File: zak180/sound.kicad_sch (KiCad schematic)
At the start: 1 part, among them U3 PSG_AY-3-8912

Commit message: HW: Further work on schematic
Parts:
- added C23, C24, C25, C26: 100n, Capacitor_THT:C_Disc_D5.0mm_W2.5mm_P2.50mm, symbol Device:C
- added C27: 47n, Capacitor_THT:C_Disc_D5.0mm_W2.5mm_P2.50mm, symbol Device:C
- added C28, C30, C31: 150u, symbol Device:C_Polarized
- added C29: 22u, symbol Device:C_Polarized
- added J4: Conn_01x02_Pin, Connector_PinHeader_1.00mm:PinHeader_1x02_P1.00mm_Vertical, symbol Connector:Conn_01x02_Pin
- added R26, R27, R28: 2K2, Resistor_THT:R_Axial_DIN0207_L6.3mm_D2.5mm_P7.62mm_Horizontal, symbol Device:R
- added R29: 10R, Resistor_THT:R_Axial_DIN0207_L6.3mm_D2.5mm_P7.62mm_Horizontal, symbol Device:R
- added RV1: 1K, symbol Device:R_Potentiometer
- added U11: 74HC02, Package_DIP:DIP-14_W7.62mm, symbol 74xx:74HC02
- added U16: 74HC08, Package_DIP:DIP-14_W7.62mm, symbol 74xx:74LS08
- added U17: LM386, symbol Amplifier_Audio:LM386
- U3: footprint (none) -> Package_DIP:DIP-28_W15.24mm
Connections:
- net GND: now also C23.2, C24.2, C25.2, C26.2, C30.1, C31.1, J4.1 (Pin_1), R29.1, RV1.3, U11.7 (GND), U16.7 (GND), U17.2 (-), U17.4 (GND)
- net VCC: now also U3.17 (A8), U3.19 (BC2), C23.1, C24.1, C25.1, C26.1, C30.2, C31.2, U11.14 (VCC), U16.14 (VCC), U17.6 (V+)
- net at U3.1 (ch_C): now also R28.1
- net SCRL4: now reaches U3.10 (IOA4)
- net SCRL3: now reaches U3.11 (IOA3)
- net SCRL2: now reaches U3.12 (IOA2)
- net SCRL1: now reaches U3.13 (IOA1)
- net SCRL0: now reaches U3.14 (IOA0)
- net CLK: now reaches U3.15 (CLOCK)
- net ~{RST}: now reaches U3.16 (~{RESET})
- net at U3.18 (BDIR): now also U11.1
- net at U3.20 (BC1): now also U11.13
- net at U3.4 (ch_B): now also R27.1
- net at U3.5 (ch_A): now also R26.1
- net ROMSEL1: now reaches U3.7 (IOA7)
- net ROMSEL0: now reaches U3.8 (IOA6)
- net SCRL5: now reaches U3.9 (IOA5)
- new net: R26.2, R27.2, R28.2, RV1.1
- new net: C29.1, RV1.2
- new net: U11.12, U16.3
- new net: C28.2, J4.2 (Pin_2)
- new net: C27.2, R29.2
- new net: C29.2, U17.3 (+)
- new net: C27.1, C28.1, U17.5
- new net: U11.10, U11.11
- new net: U11.4, U11.8, U11.9
- new net A0: U11.6
- new net ~{CS}: U11.3, U11.5
- new net ~{RD}: U16.2
- new net ~{WR}: U11.2, U16.1
- no-connect marks 0 -> 4

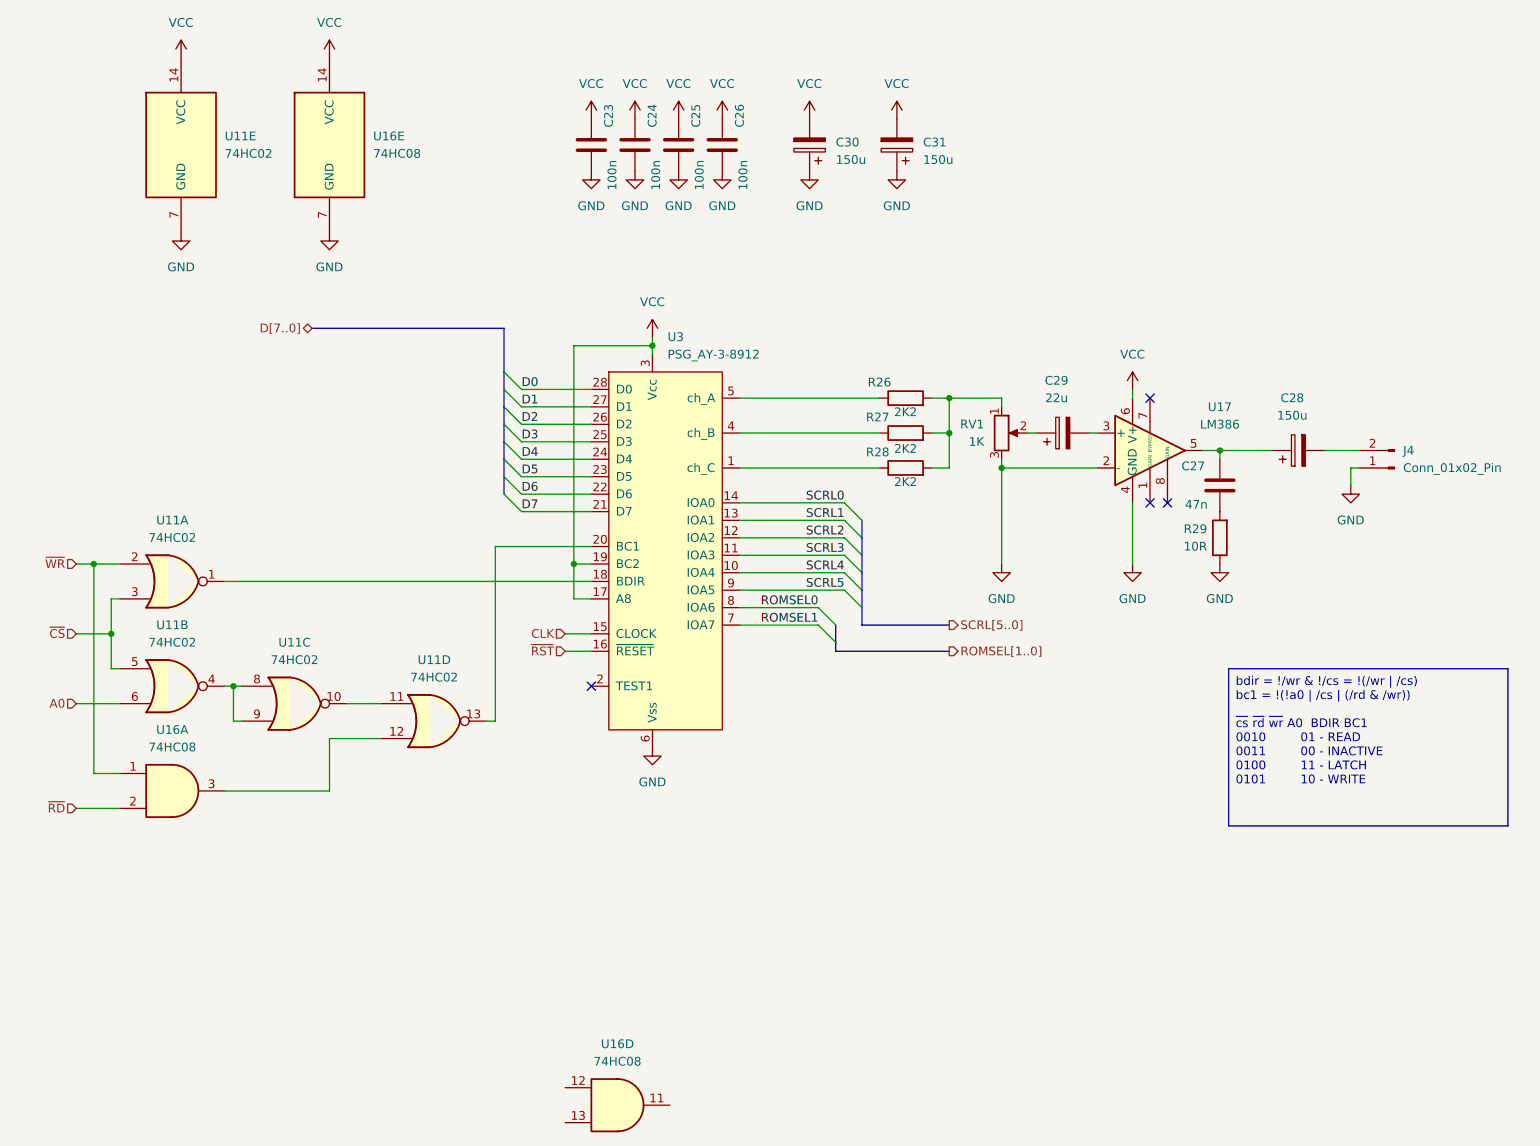
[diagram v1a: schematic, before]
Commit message: HW: Add memory, serial and power
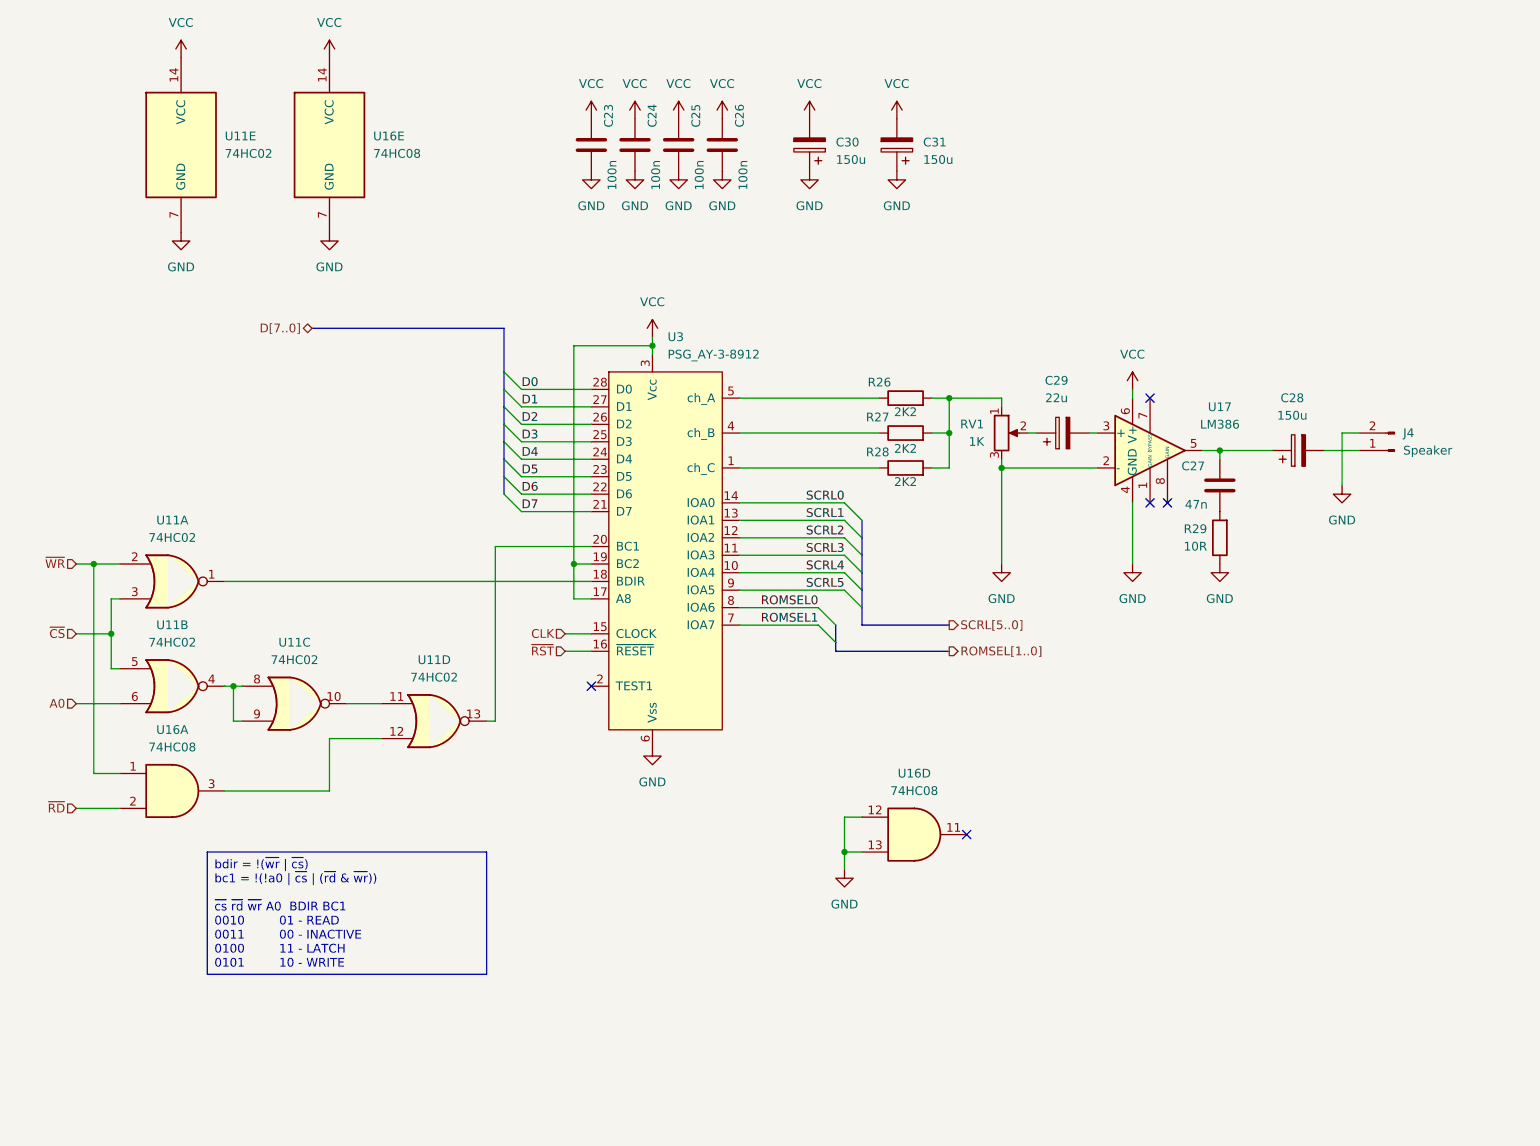
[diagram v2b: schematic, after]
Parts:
- J4: value Conn_01x02_Pin -> Speaker
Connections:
- net GND: now also J4.2 (Pin_2), U16.12, U16.13; no longer J4.1 (Pin_1)
- net at C28.2: now also J4.1 (Pin_1); no longer J4.2 (Pin_2)
- no-connect marks 4 -> 5
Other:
- moved on the sheet: J4, U16D
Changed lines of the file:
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@@
 	)
 	(junction
+		(at 158.75 142.24)
+		(diameter 0)
+		(color 0 0 0 0)
+	)
+	(junction
 		(at 173.99 81.28)
 		(diameter 0)
@@
 	)
 	(no_connect
+		(at 176.53 139.7)
+	)
+	(no_connect
 		(at 121.92 118.11)
 	)
@@
 	(wire
 		(pts
-			(xy 232.41 88.9) (xy 232.41 86.36)
-		)
-		(stroke
-			(width 0)
-			(type default)
-		)
-	)
-	(wire
-		(pts
 			(xy 143.51 99.06) (xy 158.75 99.06)
 		)
@@
 	(wire
 		(pts
-			(xy 232.41 86.36) (xy 233.68 86.36)
+			(xy 228.6 83.82) (xy 233.68 83.82)
 		)
 		(stroke
@@
 	(wire
 		(pts
+			(xy 158.75 142.24) (xy 158.75 137.16)
+		)
+		(stroke
+			(width 0)
+			(type default)
+		)
+	)
+	(wire
+		(pts
 			(xy 181.61 76.2) (xy 181.61 77.47)
 		)
@@
 	(wire
 		(pts
+			(xy 158.75 137.16) (xy 161.29 137.16)
+		)
+		(stroke
+			(width 0)
+			(type default)
+		)
+	)
+	(wire
+		(pts
 			(xy 173.99 81.28) (xy 173.99 76.2)
 		)
@@
 		)
 	)
+	(wire
+		(pts
+			(xy 231.14 88.9) (xy 231.14 81.28)
+		)
+		(stroke
+			(width 0)
+			(type default)
+		)
+	)
 	(bus
 		(pts
@@
 	(wire
 		(pts
-			(xy 228.6 83.82) (xy 233.68 83.82)
+			(xy 49.53 100.33) (xy 53.34 100.33)
 		)
 		(stroke
@@
 	(wire
 		(pts
-			(xy 49.53 100.33) (xy 53.34 100.33)
+			(xy 118.11 110.49) (xy 121.92 110.49)
 		)
 		(stroke
@@
 	(wire
 		(pts
-			(xy 118.11 110.49) (xy 121.92 110.49)
+			(xy 200.66 91.44) (xy 200.66 100.33)
 		)
 		(stroke
@@
 	(wire
 		(pts
-			(xy 200.66 91.44) (xy 200.66 100.33)
+			(xy 121.92 105.41) (xy 119.38 105.41)
 		)
 		(stroke
@@
 	(wire
 		(pts
-			(xy 121.92 105.41) (xy 119.38 105.41)
+			(xy 86.36 120.65) (xy 91.44 120.65)
 		)
 		(stroke
@@
 	(wire
 		(pts
-			(xy 86.36 120.65) (xy 91.44 120.65)
+			(xy 158.75 142.24) (xy 161.29 142.24)
+		)
+		(stroke
+			(width 0)
+			(type default)
+		)
+	)
+	(wire
+		(pts
+			(xy 231.14 81.28) (xy 233.68 81.28)
 		)
 		(stroke
@@
 	(wire
 		(pts
+			(xy 158.75 144.78) (xy 158.75 142.24)
+		)
+		(stroke
+			(width 0)
+			(type default)
+		)
+	)
+	(wire
+		(pts
 			(xy 119.38 68.58) (xy 119.38 100.33)
 		)
@@
 		)
 	)
-	(text_box "bdir = !/wr & !/cs = !(/wr | /cs)\nbc1 = !(!a0 | /cs | (/rd & /wr))\n\n~{cs} ~{rd} ~{wr} A0  BDIR BC1\n0010         01 - READ\n0011         00 - INACTIVE\n0100         11 - LATCH\n0101         10 - WRITE"
+	(text_box "bdir = !(~{wr} | ~{cs})\nbc1 = !(!a0 | ~{cs} | (~{rd} & ~{wr}))\n\n~{cs} ~{rd} ~{wr} A0  BDIR BC1\n0010         01 - READ\n0011         00 - INACTIVE\n0100         11 - LATCH\n0101         10 - WRITE"
 		(exclude_from_sim no)
-		(at 214.63 115.57 0)
-		(size 40.64 22.86)
+		(at 66.04 142.24 0)
+		(size 40.64 17.78)
 		(stroke
 			(width 0)
@@
 	(symbol
 		(lib_id "power:GND")
-		(at 232.41 88.9 0)
+		(at 231.14 88.9 0)
 		(unit 1)
 		(exclude_from_sim no)
@@
 		(fields_autoplaced yes)
 		(property "Reference" "#PWR0100"
-			(at 232.41 95.25 0)
+			(at 231.14 95.25 0)
 			(effects
 				(font
@@
 		)
 		(property "Value" "GND"
-			(at 232.41 93.98 0)
+			(at 231.14 93.98 0)
 			(effects
 				(font
@@
 		)
 		(property "Footprint" ""
-			(at 232.41 88.9 0)
+			(at 231.14 88.9 0)
 			(effects
 				(font
@@
 		)
 		(property "Datasheet" ""
-			(at 232.41 88.9 0)
+			(at 231.14 88.9 0)
 			(effects
 				(font
@@
 		)
 		(property "Description" "Power symbol creates a global label with name \"GND\" , ground"
-			(at 232.41 88.9 0)
+			(at 231.14 88.9 0)
 			(effects
 				(font
@@
 	(symbol
 		(lib_id "Connector:Conn_01x02_Pin")
-		(at 238.76 86.36 180)
+		(at 238.76 83.82 180)
 		(unit 1)
 		(exclude_from_sim no)
@@
 		(fields_autoplaced yes)
 		(property "Reference" "J4"
-			(at 240.03 83.8199 0)
+			(at 240.03 81.2799 0)
 			(effects
 				(font
@@
 			)
 		)
-		(property "Value" "Conn_01x02_Pin"
-			(at 240.03 86.3599 0)
+		(property "Value" "Speaker"
+			(at 240.03 83.8199 0)
 			(effects
 				(font
@@
 		)
 		(property "Footprint" "Connector_PinHeader_1.00mm:PinHeader_1x02_P1.00mm_Vertical"
-			(at 238.76 86.36 0)
+			(at 238.76 83.82 0)
 			(effects
 				(font
@@
 		)
 		(property "Datasheet" "~"
-			(at 238.76 86.36 0)
+			(at 238.76 83.82 0)
 			(effects
 				(font
@@
 		)
 		(property "Description" "Generic connector, single row, 01x02, script generated"
-			(at 238.76 86.36 0)
+			(at 238.76 83.82 0)
 			(effects
 				(font
@@
 	(symbol
 		(lib_id "74xx:74LS08")
-		(at 125.73 179.07 0)
+		(at 168.91 139.7 0)
 		(unit 4)
 		(exclude_from_sim no)
@@
 		(fields_autoplaced yes)
 		(property "Reference" "U16"
-			(at 125.7217 170.18 0)
+			(at 168.9017 130.81 0)
 			(effects
 				(font
@@
 		)
 		(property "Value" "74HC08"
-			(at 125.7217 172.72 0)
+			(at 168.9017 133.35 0)
 			(effects
 				(font
@@
 		)
 		(property "Footprint" "Package_DIP:DIP-14_W7.62mm"
-			(at 125.73 179.07 0)
+			(at 168.91 139.7 0)
 			(effects
 				(font
@@
 		)
 		(property "Datasheet" "http://www.ti.com/lit/gpn/sn74LS08"
-			(at 125.73 179.07 0)
+			(at 168.91 139.7 0)
 			(effects
 				(font
@@
 		)
 		(property "Description" "Quad And2"
-			(at 125.73 179.07 0)
+			(at 168.91 139.7 0)
 			(effects
 				(font
@@
 				)
 			)
+		)
+	)
+	(symbol
+		(lib_id "power:GND")
+		(at 158.75 144.78 0)
+		(unit 1)
+		(exclude_from_sim no)
+		(in_bom yes)
+		(on_board yes)
+		(dnp no)
+		(fields_autoplaced yes)
+		(property "Reference" "#PWR0166"
+			(at 158.75 151.13 0)
+			(effects
+				(font
+					(size 1.27 1.27)
+				)
+				(hide yes)
+			)
+		)
+		(property "Value" "GND"
+			(at 158.75 149.86 0)
+			(effects
+				(font
+					(size 1.27 1.27)
+				)
+			)
+		)
+		(property "Footprint" ""
+			(at 158.75 144.78 0)
+			(effects
+				(font
+					(size 1.27 1.27)
+				)
+				(hide yes)
+			)
+		)
+		(property "Datasheet" ""
+			(at 158.75 144.78 0)
+			(effects
+				(font
+					(size 1.27 1.27)
+				)
+				(hide yes)
+			)
+		)
+		(property "Description" "Power symbol creates a global label with name \"GND\" , ground"
+			(at 158.75 144.78 0)
+			(effects
+				(font
+					(size 1.27 1.27)
+				)
+				(hide yes)
+			)
+		)
+		(pin "1"
+		)
+		(instances
+			(project "zak180"
+				(path "/ca48b56d-33a4-442b-b1b9-aaf2c2c8d68d/0bc6fd8f-001b-40d5-aa7a-728fb33c946c"
+					(reference "#PWR0166")
+					(unit 1)
+				)
+			)
